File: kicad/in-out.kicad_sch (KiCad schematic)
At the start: 69 parts, among them J9 Conn_01x07, U11 LM5106MM

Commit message: Route finish
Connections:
- net +3V3 renamed +3.3V
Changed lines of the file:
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@@
     (stroke (width 0) (type default))
   )
-  (wire (pts (xy 41.91 20.32) (xy 41.91 24.13))
-    (stroke (width 0) (type default))
-  )
   (wire (pts (xy 204.47 39.37) (xy 204.47 30.48))
     (stroke (width 0) (type default))
@@
     (stroke (width 0) (type default))
   )
-  (wire (pts (xy 39.37 64.77) (xy 39.37 68.58))
-    (stroke (width 0) (type default))
-  )
   (wire (pts (xy 68.58 58.42) (xy 67.31 58.42))
     (stroke (width 0) (type default))
@@
     (stroke (width 0) (type default))
   )
-  (wire (pts (xy 196.85 78.74) (xy 196.85 81.28))
+  (wire (pts (xy 196.85 76.2) (xy 196.85 81.28))
     (stroke (width 0) (type default))
   )
@@
     (stroke (width 0) (type default))
   )
+  (wire (pts (xy 39.37 63.5) (xy 39.37 68.58))
+    (stroke (width 0) (type default))
+  )
   (wire (pts (xy 55.88 80.01) (xy 59.69 80.01))
     (stroke (width 0) (type default))
@@
     (stroke (width 0) (type default))
   )
+  (wire (pts (xy 41.91 19.05) (xy 41.91 24.13))
+    (stroke (width 0) (type default))
+  )
   (wire (pts (xy 21.59 148.59) (xy 24.13 148.59))
     (stroke (width 0) (type default))
@@
     )
   )
-  (symbol (lib_id "PCM_4ms_Power-symbol:+3.3V") (at 41.91 20.32 0) (unit 1)
-    (in_bom yes) (on_board yes) (dnp no) (fields_autoplaced)
-    (property "Reference" "#PWR?" (at 41.91 24.13 0)
-      (effects (font (size 1.27 1.27)) hide)
-    )
-    (property "Value" "+3.3V" (at 41.91 16.51 0)
-      (effects (font (size 1.27 1.27)))
-    )
-    (property "Footprint" "" (at 41.91 20.32 0)
-      (effects (font (size 1.27 1.27)) hide)
-    )
-    (property "Datasheet" "" (at 41.91 20.32 0)
-      (effects (font (size 1.27 1.27)) hide)
-    )
-    (pin "1")
-    (instances
-      (project "in-out"
-        (path "/00132dca-dc65-4fe2-9a8e-5357fa3abe75"
-          (reference "#PWR?") (unit 1)
-        )
-      )
-      (project "jbc_station"
-        (path "/d4547348-927f-40d5-95cc-3315216c85d1/20d00893-b9a1-4c38-a3cb-53ca590a39ee"
-          (reference "#PWR052") (unit 1)
-        )
-        (path "/d4547348-927f-40d5-95cc-3315216c85d1/1e973139-bece-4819-8007-ddc7a1cb74ce"
-          (reference "#PWR074") (unit 1)
-        )
-        (path "/d4547348-927f-40d5-95cc-3315216c85d1/2d95b73f-9845-4f86-b3aa-b18e657d0fbf"
-          (reference "#PWR096") (unit 1)
-        )
-      )
-    )
-  )
   (symbol (lib_id "Device:R") (at 107.95 64.77 90) (unit 1)
     (in_bom yes) (on_board yes) (dnp no)
@@
     )
   )
-  (symbol (lib_id "PCM_4ms_Power-symbol:+3.3V") (at 196.85 78.74 0) (unit 1)
-    (in_bom yes) (on_board yes) (dnp no) (fields_autoplaced)
-    (property "Reference" "#PWR?" (at 196.85 82.55 0)
-      (effects (font (size 1.27 1.27)) hide)
-    )
-    (property "Value" "+3.3V" (at 196.85 74.93 0)
-      (effects (font (size 1.27 1.27)))
-    )
-    (property "Footprint" "" (at 196.85 78.74 0)
-      (effects (font (size 1.27 1.27)) hide)
-    )
-    (property "Datasheet" "" (at 196.85 78.74 0)
-      (effects (font (size 1.27 1.27)) hide)
-    )
-    (pin "1")
-    (instances
-      (project "in-out"
-        (path "/00132dca-dc65-4fe2-9a8e-5357fa3abe75"
-          (reference "#PWR?") (unit 1)
-        )
-      )
-      (project "jbc_station"
-        (path "/d4547348-927f-40d5-95cc-3315216c85d1/20d00893-b9a1-4c38-a3cb-53ca590a39ee"
-          (reference "#PWR063") (unit 1)
-        )
-        (path "/d4547348-927f-40d5-95cc-3315216c85d1/1e973139-bece-4819-8007-ddc7a1cb74ce"
-          (reference "#PWR085") (unit 1)
-        )
-        (path "/d4547348-927f-40d5-95cc-3315216c85d1/2d95b73f-9845-4f86-b3aa-b18e657d0fbf"
-          (reference "#PWR0107") (unit 1)
-        )
-      )
-    )
-  )
   (symbol (lib_id "Diode_TVS_AKL:ESD5Z3V3") (at 30.48 87.63 90) (unit 1)
     (in_bom yes) (on_board yes) (dnp no)
@@
     )
   )
+  (symbol (lib_id "power:+3.3V") (at 39.37 63.5 0) (unit 1)
+    (in_bom yes) (on_board yes) (dnp no)
+    (property "Reference" "#PWR026" (at 39.37 67.31 0)
+      (effects (font (size 1.27 1.27)) hide)
+    )
+    (property "Value" "+3.3V" (at 41.91 59.69 0)
+      (effects (font (size 1.27 1.27)))
+    )
+    (property "Footprint" "" (at 39.37 63.5 0)
+      (effects (font (size 1.27 1.27)) hide)
+    )
+    (property "Datasheet" "" (at 39.37 63.5 0)
+      (effects (font (size 1.27 1.27)) hide)
+    )
+    (pin "1")
+    (instances
+      (project "jbc_station"
+        (path "/d4547348-927f-40d5-95cc-3315216c85d1"
+          (reference "#PWR026") (unit 1)
+        )
+        (path "/d4547348-927f-40d5-95cc-3315216c85d1/20d00893-b9a1-4c38-a3cb-53ca590a39ee"
+          (reference "#PWR058") (unit 1)
+        )
+        (path "/d4547348-927f-40d5-95cc-3315216c85d1/1e973139-bece-4819-8007-ddc7a1cb74ce"
+          (reference "#PWR080") (unit 1)
+        )
+        (path "/d4547348-927f-40d5-95cc-3315216c85d1/2d95b73f-9845-4f86-b3aa-b18e657d0fbf"
+          (reference "#PWR096") (unit 1)
+        )
+      )
+    )
+  )
   (symbol (lib_id "Device:R") (at 90.17 156.21 90) (unit 1)
     (in_bom yes) (on_board no) (dnp no)
@@
     )
   )
+  (symbol (lib_id "power:+3.3V") (at 41.91 19.05 0) (unit 1)
+    (in_bom yes) (on_board yes) (dnp no)
+    (property "Reference" "#PWR026" (at 41.91 22.86 0)
+      (effects (font (size 1.27 1.27)) hide)
+    )
+    (property "Value" "+3.3V" (at 44.45 15.24 0)
+      (effects (font (size 1.27 1.27)))
+    )
+    (property "Footprint" "" (at 41.91 19.05 0)
+      (effects (font (size 1.27 1.27)) hide)
+    )
+    (property "Datasheet" "" (at 41.91 19.05 0)
+      (effects (font (size 1.27 1.27)) hide)
+    )
+    (pin "1")
+    (instances
+      (project "jbc_station"
+        (path "/d4547348-927f-40d5-95cc-3315216c85d1"
+          (reference "#PWR026") (unit 1)
+        )
+        (path "/d4547348-927f-40d5-95cc-3315216c85d1/20d00893-b9a1-4c38-a3cb-53ca590a39ee"
+          (reference "#PWR046") (unit 1)
+        )
+        (path "/d4547348-927f-40d5-95cc-3315216c85d1/1e973139-bece-4819-8007-ddc7a1cb74ce"
+          (reference "#PWR052") (unit 1)
+        )
+        (path "/d4547348-927f-40d5-95cc-3315216c85d1/2d95b73f-9845-4f86-b3aa-b18e657d0fbf"
+          (reference "#PWR074") (unit 1)
+        )
+      )
+    )
+  )
   (symbol (lib_id "Connector:DIN-5") (at 90.17 173.99 0) (mirror y) (unit 1)
     (in_bom yes) (on_board no) (dnp no)
@@
     )
   )
-  (symbol (lib_id "PCM_4ms_Power-symbol:+3.3V") (at 39.37 64.77 0) (unit 1)
-    (in_bom yes) (on_board yes) (dnp no) (fields_autoplaced)
-    (property "Reference" "#PWR?" (at 39.37 68.58 0)
-      (effects (font (size 1.27 1.27)) hide)
-    )
-    (property "Value" "+3.3V" (at 39.37 60.96 0)
-      (effects (font (size 1.27 1.27)))
-    )
-    (property "Footprint" "" (at 39.37 64.77 0)
-      (effects (font (size 1.27 1.27)) hide)
-    )
-    (property "Datasheet" "" (at 39.37 64.77 0)
-      (effects (font (size 1.27 1.27)) hide)
-    )
-    (pin "1")
-    (instances
-      (project "in-out"
-        (path "/00132dca-dc65-4fe2-9a8e-5357fa3abe75"
-          (reference "#PWR?") (unit 1)
-        )
-      )
-      (project "jbc_station"
-        (path "/d4547348-927f-40d5-95cc-3315216c85d1/20d00893-b9a1-4c38-a3cb-53ca590a39ee"
-          (reference "#PWR058") (unit 1)
-        )
-        (path "/d4547348-927f-40d5-95cc-3315216c85d1/1e973139-bece-4819-8007-ddc7a1cb74ce"
-          (reference "#PWR080") (unit 1)
-        )
-        (path "/d4547348-927f-40d5-95cc-3315216c85d1/2d95b73f-9845-4f86-b3aa-b18e657d0fbf"
-          (reference "#PWR0102") (unit 1)
-        )
-      )
-    )
-  )
   (symbol (lib_id "Device:C_Polarized") (at 130.81 55.88 0) (unit 1)
     (in_bom yes) (on_board yes) (dnp no)
@@
         )
       )
+    )
+  )
+  (symbol (lib_id "power:+3.3V") (at 196.85 76.2 0) (unit 1)
+    (in_bom yes) (on_board yes) (dnp no)
+    (property "Reference" "#PWR026" (at 196.85 80.01 0)
+      (effects (font (size 1.27 1.27)) hide)
+    )
+    (property "Value" "+3.3V" (at 199.39 72.39 0)
+      (effects (font (size 1.27 1.27)))
+    )
+    (property "Footprint" "" (at 196.85 76.2 0)
+      (effects (font (size 1.27 1.27)) hide)
+    )
+    (property "Datasheet" "" (at 196.85 76.2 0)
+      (effects (font (size 1.27 1.27)) hide)
+    )
+    (pin "1")
+    (instances
+      (project "jbc_station"
+        (path "/d4547348-927f-40d5-95cc-3315216c85d1"
+          (reference "#PWR026") (unit 1)
+        )
+        (path "/d4547348-927f-40d5-95cc-3315216c85d1/20d00893-b9a1-4c38-a3cb-53ca590a39ee"
+          (reference "#PWR063") (unit 1)
+        )
+        (path "/d4547348-927f-40d5-95cc-3315216c85d1/1e973139-bece-4819-8007-ddc7a1cb74ce"
+          (reference "#PWR085") (unit 1)
+        )
+        (path "/d4547348-927f-40d5-95cc-3315216c85d1/2d95b73f-9845-4f86-b3aa-b18e657d0fbf"
+          (reference "#PWR0102") (unit 1)
+        )
+      )

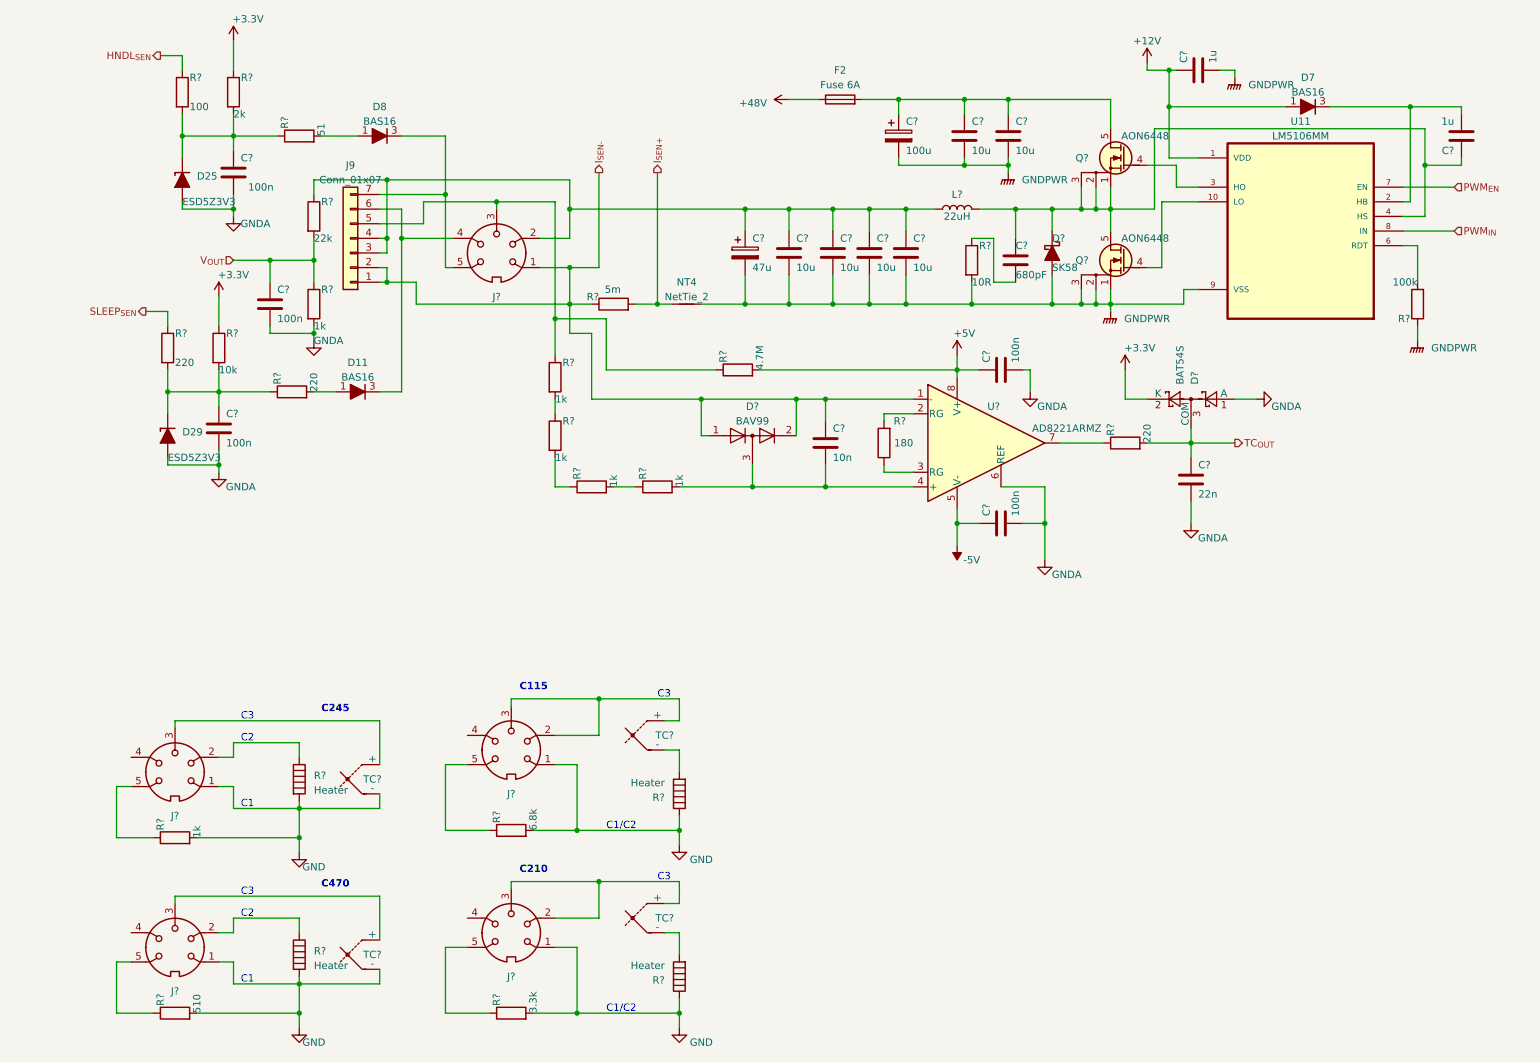
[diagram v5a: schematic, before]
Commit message: Add more filtering caps for ADC
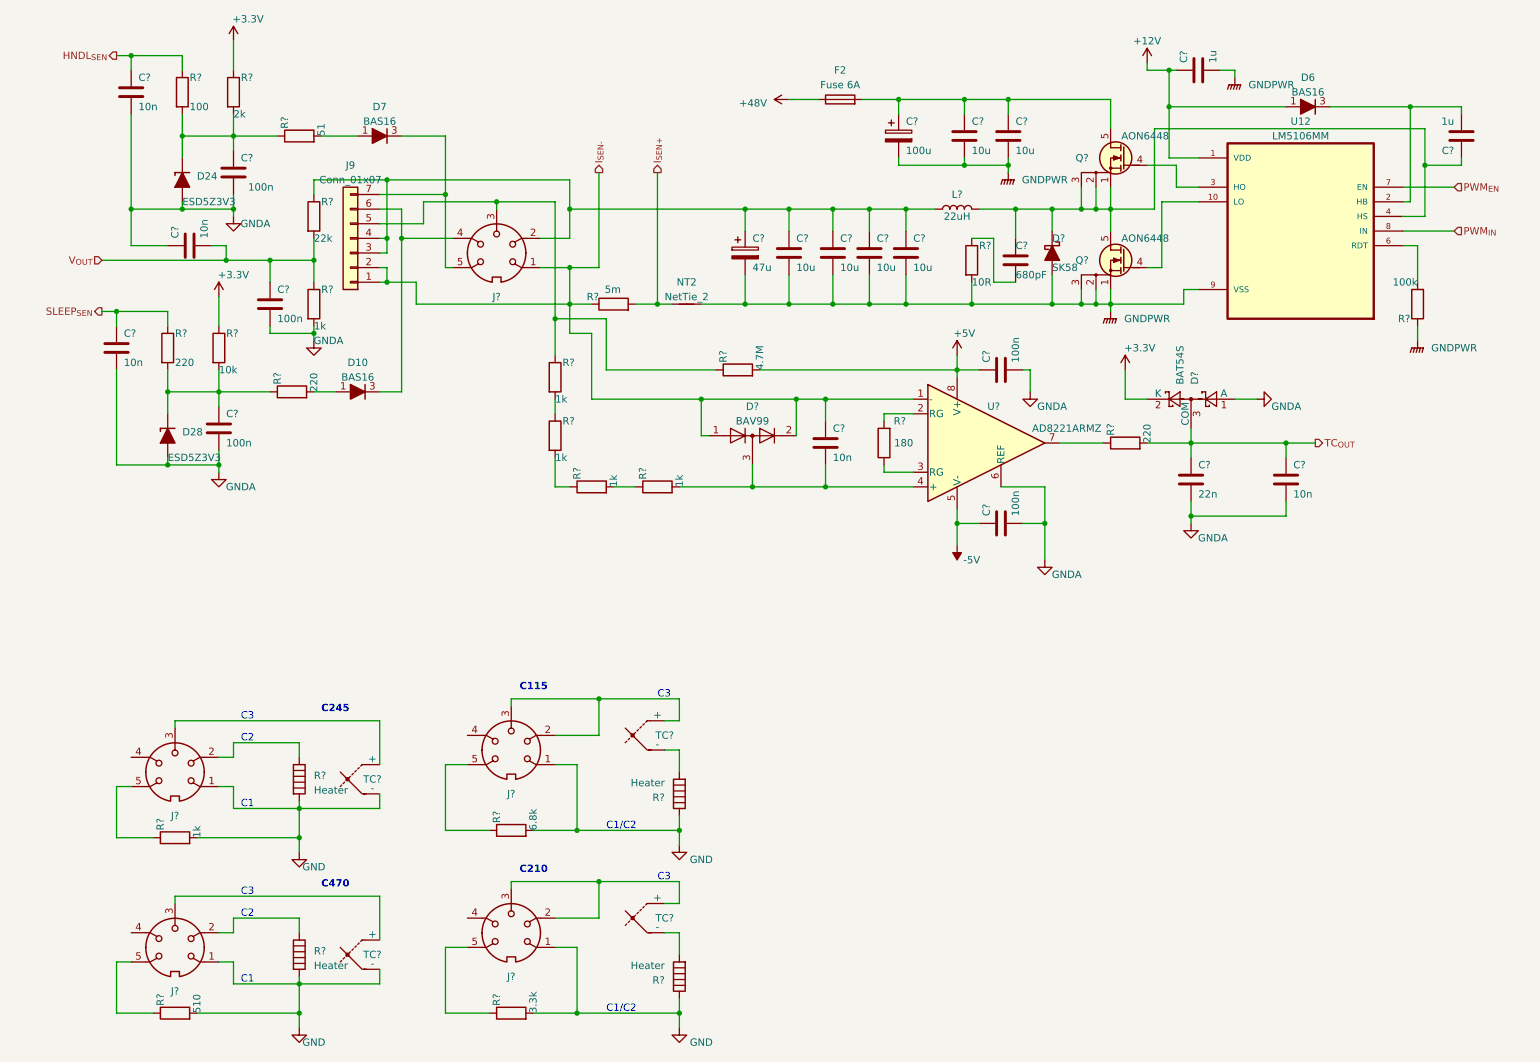
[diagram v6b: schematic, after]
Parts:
- added C? (x4): 10n, Capacitor_SMD:C_0402_1005Metric, symbol Device:C
- renumbered D11 to D10, D25 to D24, D29 to D28, D7 to D6, D8 to D7, NT4 to NT2, U11 to U12
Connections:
- net GNDA: now also C?.1, C?.2, C?.2, C?.2
- net HNDL_{SEN}: now also C?.1
- net SLEEP_{SEN}: now also C?.1
- net TC_{OUT}: now also C?.1
- net V_{OUT}: now also C?.2
